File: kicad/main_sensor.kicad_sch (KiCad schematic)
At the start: 48 parts, among them J2 L17DEFRA09S, J7 N2510-6002-RB, U11 THS4561IDGKx, U4 ADR4540BRZ, U5 ADA4895-1ARJZ, U7 LTC2380CMS-24#PBF

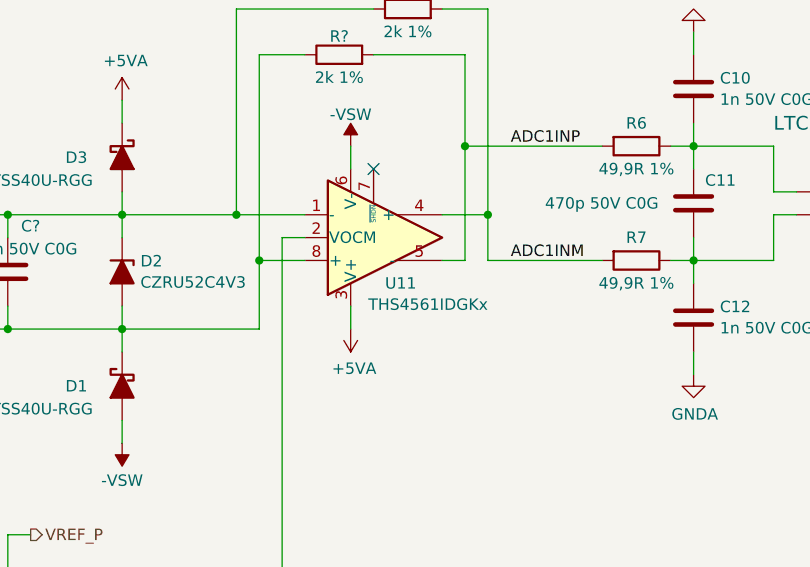
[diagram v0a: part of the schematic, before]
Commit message: bugfix: driver for 4th T, capacitors for input amps
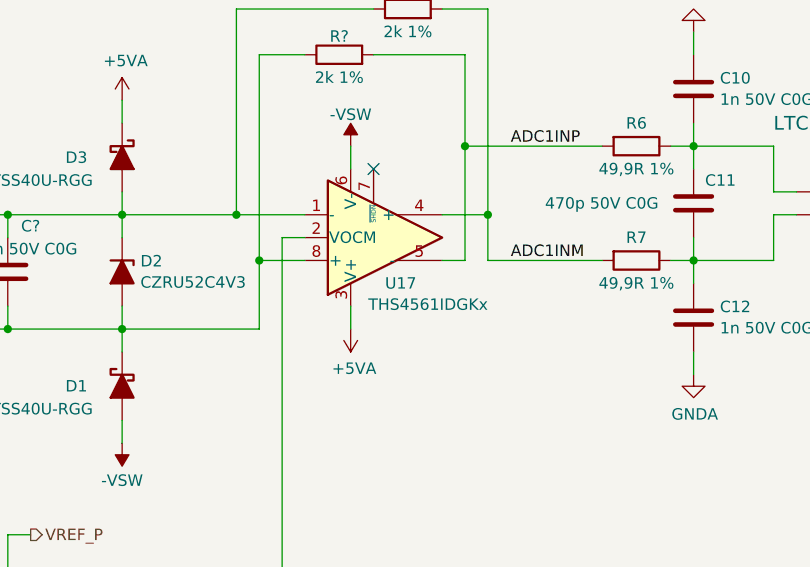
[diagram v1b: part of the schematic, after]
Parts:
- C19, C22, C24, C29, C39: value GCM31CR71C106KA64L -> GCM31CR71C106KA64L
- U4: value ADR4540BRZ -> ADR4540BRZ
- U7: value LTC2380CMS-24#PBF -> LTC2380CMS-24#PBF
- renumbered U11 to U17
